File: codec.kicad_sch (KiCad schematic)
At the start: 23 parts, among them CN1 IN, CN2 OUT, U15 TAC5111IRGER, U17 LM321, U18 TPA6130A2RTJR

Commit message: wip 3.5mm audio jacks
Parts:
- added C50: 10nF, Capacitor_SMD:C_0402_1005Metric, symbol Device:C_Small
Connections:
- net GND: now also CN1.1
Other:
- moved on the sheet: CN1
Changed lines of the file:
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@@
 	(wire
 		(pts
+			(xy 38.1 162.56) (xy 40.64 162.56)
+		)
+		(stroke
+			(width 0)
+			(type default)
+		)
+	)
+	(wire
+		(pts
 			(xy 139.7 86.36) (xy 137.16 86.36)
 		)
@@
 	(symbol
 		(lib_id "custom:PJ-3537S")
-		(at 46.99 166.37 0)
+		(at 31.75 166.37 0)
 		(unit 1)
 		(body_style 1)
@@
 		(fields_autoplaced yes)
 		(property "Reference" "CN1"
-			(at 44.83 157.48 0)
+			(at 29.59 157.48 0)
 			(show_name no)
 			(do_not_autoplace no)
@@
 		)
 		(property "Value" "IN"
-			(at 44.83 160.02 0)
+			(at 29.59 160.02 0)
 			(show_name no)
 			(do_not_autoplace no)
@@
 		)
 		(property "Footprint" "custom:AUDIO-SMD_PJ-3537S"
-			(at 46.99 180.34 0)
+			(at 31.75 180.34 0)
 			(hide yes)
 			(show_name no)
@@
 		)
 		(property "Datasheet" "https://www.lcsc.com/datasheet/C2689709.pdf"
-			(at 46.99 182.88 0)
+			(at 31.75 182.88 0)
 			(hide yes)
 			(show_name no)
@@
 		)
 		(property "Description" ""
-			(at 46.99 166.37 0)
+			(at 31.75 166.37 0)
 			(hide yes)
 			(show_name no)
@@
 		)
 		(property "Manufacturer" "XKB Connection(中国星坤)"
-			(at 46.99 185.42 0)
+			(at 31.75 185.42 0)
 			(hide yes)
 			(show_name no)
@@
 		)
 		(property "MPN" "PJ-3537S-SMT"
-			(at 46.99 187.96 0)
+			(at 31.75 187.96 0)
 			(hide yes)
 			(show_name no)
@@
 		)
 		(property "LCSC Part" "C2689709"
-			(at 46.99 190.5 0)
+			(at 31.75 190.5 0)
 			(hide yes)
 			(show_name no)
@@
 		)
 		(property "LCSC" "C2689709"
-			(at 46.99 195.58 0)
+			(at 31.75 195.58 0)
 			(hide yes)
 			(show_name no)
@@
 	)
 	(symbol
+		(lib_id "Device:C_Small")
+		(at 66.04 185.42 90)
+		(unit 1)
+		(body_style 1)
+		(exclude_from_sim no)
+		(in_bom yes)
+		(on_board yes)
+		(in_pos_files yes)
+		(dnp no)
+		(property "Reference" "C50"
+			(at 66.0807 182.4637 90)
+			(show_name no)
+			(do_not_autoplace no)
+			(effects
+				(font
+					(size 1.27 1.27)
+				)
+			)
+		)
+		(property "Value" "10nF"
+			(at 66.0807 188.6269 90)
+			(show_name no)
+			(do_not_autoplace no)
+			(effects
+				(font
+					(size 1.27 1.27)
+				)
+			)
+		)
+		(property "Footprint" "Capacitor_SMD:C_0402_1005Metric"
+			(at 66.04 185.42 0)
+			(hide yes)
+			(show_name no)
+			(do_not_autoplace no)
+			(effects
+				(font
+					(size 1.27 1.27)
+				)
+			)
+		)
+		(property "Datasheet" ""
+			(at 66.04 185.42 0)
+			(hide yes)
+			(show_name no)
+			(do_not_autoplace no)
+			(effects
+				(font
+					(size 1.27 1.27)
+				)
+			)
+		)
+		(property "Description" "Unpolarized capacitor, small symbol"
+			(at 66.04 185.42 0)
+			(hide yes)
+			(show_name no)
+			(do_not_autoplace no)
+			(effects
+				(font
+					(size 1.27 1.27)
+				)
+			)
+		)
+		(property "LCSC" "C15195"
+			(at 66.04 185.42 0)
+			(hide yes)
+			(show_name no)
+			(do_not_autoplace no)
+			(effects
+				(font
+					(size 1.27 1.27)
+				)
+			)
+		)
+		(property "Voltage" "50V"
+			(at 66.04 185.42 90)
+			(hide yes)
+			(show_name no)
+			(do_not_autoplace no)
+			(effects
+				(font
+					(size 1.27 1.27)
+				)
+			)
+		)
+		(pin "1"
+		)
+		(pin "2"
+		)
+		(instances
+			(project "pedal"
+				(path "/e2443317-b83f-4e66-ac79-3186c6d613f3/a1bbde72-fd3e-4fef-8e82-ce5db1c82ed5"
+					(reference "C50")
+					(unit 1)
+				)
+			)
+		)
+	)
+	(symbol
 		(lib_id "power:GND")
 		(at 228.6 121.92 0)
@@
 	(symbol
 		(lib_id "power:GND")
-		(at 55.88 175.26 0)
-		(mirror y)
+		(at 40.64 162.56 90)
+		(mirror x)
 		(unit 1)
 		(body_style 1)
@@
 		(fields_autoplaced yes)
 		(property "Reference" "#PWR0135"
-			(at 55.88 181.61 0)
+			(at 46.99 162.56 0)
 			(hide yes)
 			(show_name no)
@@
 		)
 		(property "Value" "GND"
-			(at 55.88 180.34 0)
+			(at 44.45 162.5599 90)
 			(show_name no)
 			(do_not_autoplace no)
@@
 					(size 1.27 1.27)
 				)
+				(justify right)
 			)
 		)
 		(property "Footprint" ""
-			(at 55.88 175.26 0)
+			(at 40.64 162.56 0)
 			(hide yes)
 			(show_name no)
@@
 		)
 		(property "Datasheet" ""
-			(at 55.88 175.26 0)
+			(at 40.64 162.56 0)
 			(hide yes)
 			(show_name no)
@@
 		)
 		(property "Description" "Power symbol creates a global label with name \"GND\" , ground"
-			(at 55.88 175.26 0)
+			(at 40.64 162.56 0)
 			(hide yes)
 			(show_name no)

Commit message: FINALLY add 3.5mm audio jacks
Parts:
- removed CN1: IN, custom:AUDIO-SMD_PJ-3537S, symbol custom:PJ-3537S
- removed CN2: OUT, custom:AUDIO-SMD_PJ-3537S, symbol custom:PJ-3537S
- added C62, C63: 10nF, Capacitor_SMD:C_0402_1005Metric, symbol Device:C_Small
- added J10, J11, J9: PJ-327C-4A, custom:AUDIO-SMD_PJ-327C-4A, symbol custom:PJ-327C-4A
- added R28, R30, R31: 10k, Resistor_SMD:R_0402_1005Metric, symbol Device:R_Small
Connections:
- net GND: now also C50.2, C62.2, C63.2, J10.5 (S), J11.5 (S), J9.5 (S)
- net IN: now also J9.4 (T)
- net OUT_LEFT: now also J10.4 (T)
- net OUT_RIGHT: now also J11.4 (T)
- net at C50.1: now also J9.3 (DETECT), R28.1
- new net: C63.1, J11.3 (DETECT), R31.1
- new net: C62.1, J10.3 (DETECT), R30.1
- new net IN_DETECT: R28.2
- new net L_OUT_DETECT: R30.2
- new net R_OUT_DETECT: R31.2
- no-connect marks 5 -> 8

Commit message: OK ACTUALLY ADD JACKS
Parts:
- removed J10, J11, J9: PJ-327C-4A, custom:AUDIO-SMD_PJ-327C-4A, symbol custom:PJ-327C-4A
- added J7, J8, J9: PJ-342 141, custom:AUDIO-SMD_PJ-342-141, symbol custom:PJ-342141
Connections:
- net GND: now also J7.1 (GND), J8.1 (GND), J9.1 (GND)
- net at C63.1, R31.1: now also J9.2 (RING2)
- net at C62.1, R30.1: now also J8.2 (RING2)
- net at C50.1, R28.1: now also J7.2 (RING2)
- net IN: no longer names the net of C53.1
- net IN: now also J7.4 (TIP)
- net OUT_LEFT: no longer names the net of U18.14 (HPLEFT)
- net OUT_LEFT: now also J8.4 (TIP)
- net OUT_RIGHT: no longer names the net of U18.11 (HPRIGHT)
- net OUT_RIGHT: now also J9.4 (TIP)
- no-connect marks 8 -> 14
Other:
- note added: "Configure *_OUT_DETECT pins with internal pullups"
- moved on the sheet: C46, C47, C48, C49, C50, C51, C52, C53, C54, C55, C56, C58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

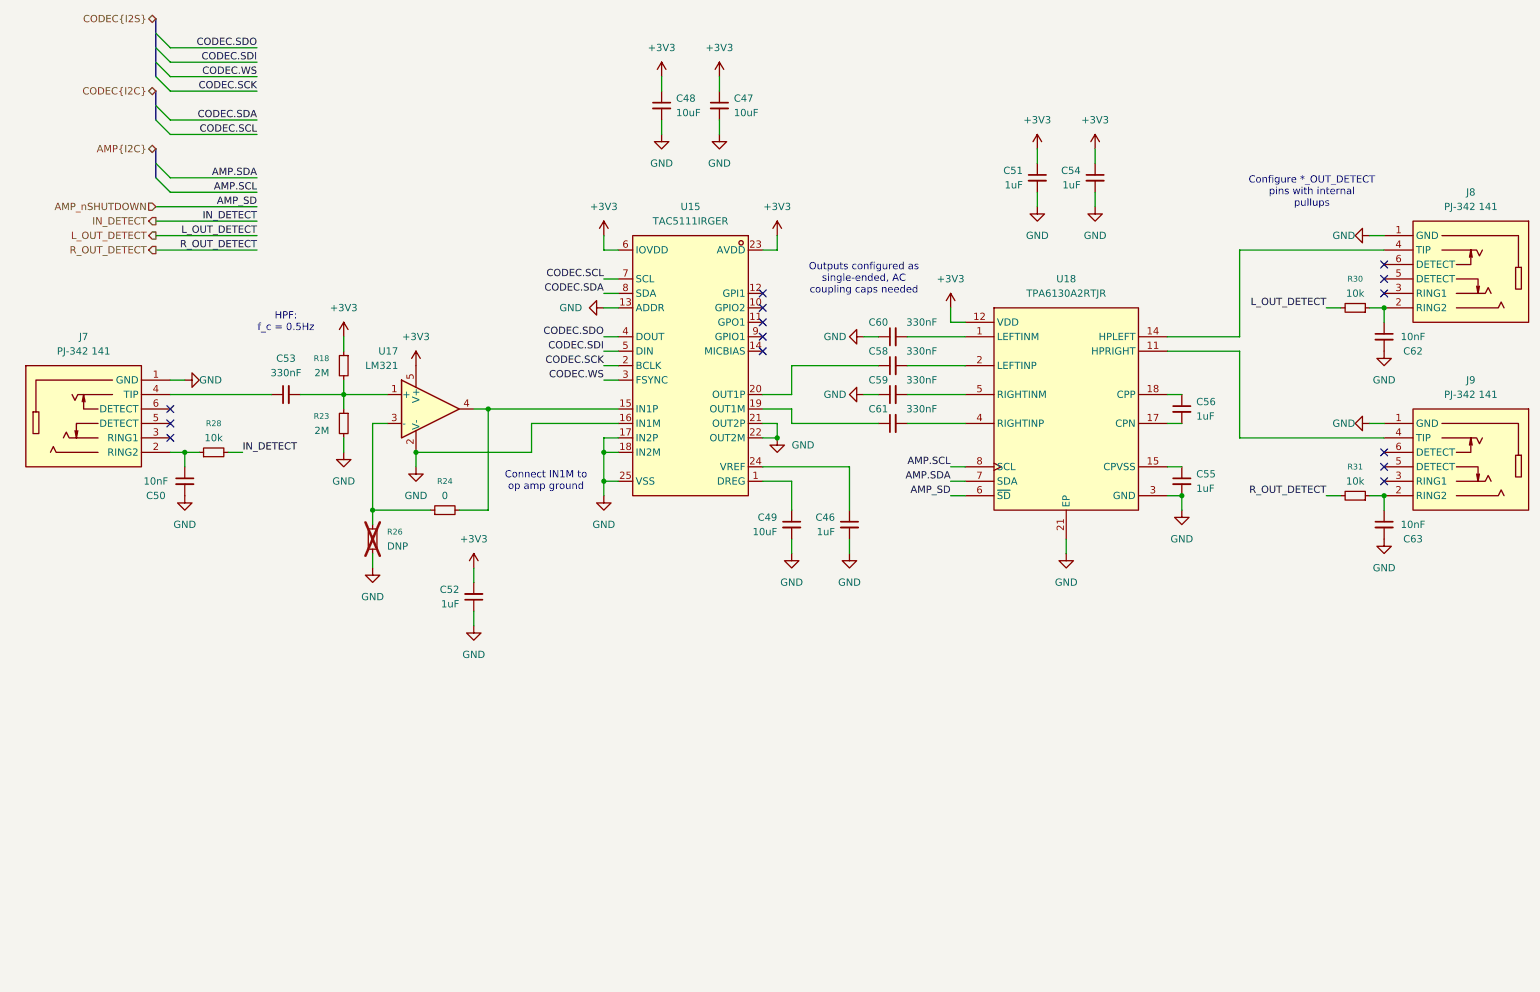
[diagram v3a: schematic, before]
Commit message: Input (#6)
* Add input subsheet
* Add debounce subsheet
* Add ultra thin buttons for ABXY
* Add start and select buttons
* Add L/R buttons
* Add joystick connector
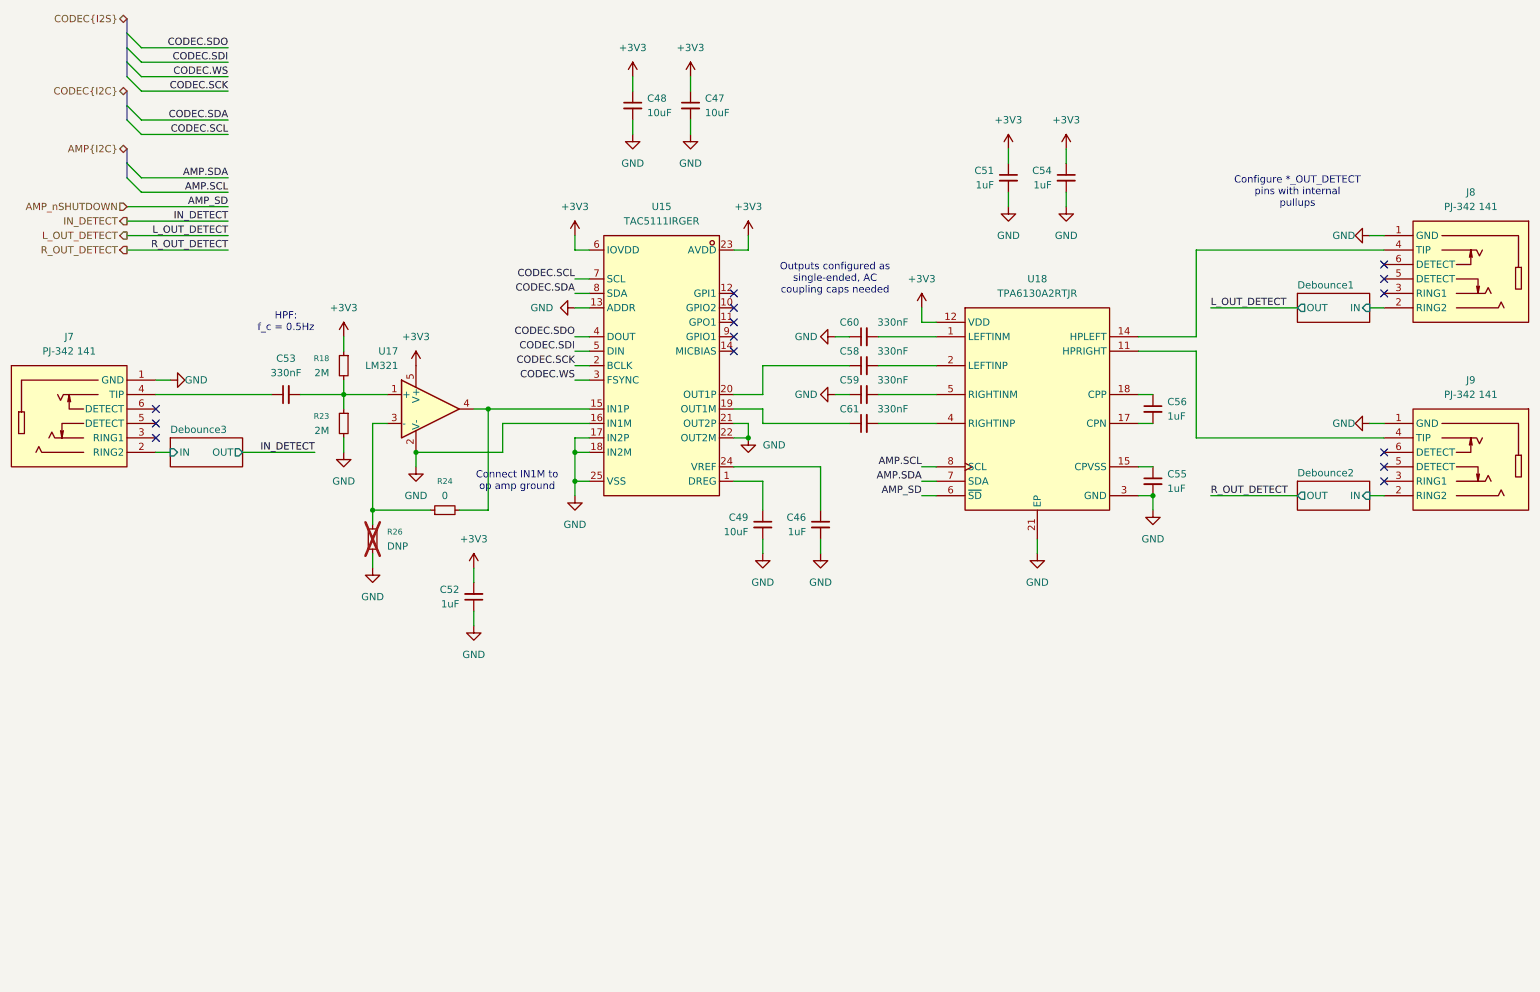
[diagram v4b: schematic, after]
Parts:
- removed C50, C62, C63: 10nF, Capacitor_SMD:C_0402_1005Metric, symbol Device:C_Small
- removed R28, R30, R31: 10k, Resistor_SMD:R_0402_1005Metric, symbol Device:R_Small
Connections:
- net Debounce2/IN: now reaches J9.2 (RING2)
- net Debounce1/IN: now reaches J8.2 (RING2)
- net Debounce3/IN: now reaches J7.2 (RING2)
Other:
- added sheet Debounce1 (debounce.kicad_sch)
- added sheet Debounce2 (debounce.kicad_sch)
- added sheet Debounce3 (debounce.kicad_sch)
- moved on the sheet: C46, C47, C48, C49, C51, C54, C55, C56, C58, C59, C60, C61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

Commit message: Move everything onto the board
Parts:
- J7: value PJ-342 141 -> IN
- J8: value PJ-342 141 -> L_OUT
- J9: value PJ-342 141 -> R_OUT
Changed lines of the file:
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@@
 		(in_pos_files yes)
 		(dnp no)
-		(fields_autoplaced yes)
 		(property "Reference" "J8"
-			(at 271.78 58.42 0)
-			(show_name no)
-			(do_not_autoplace no)
-			(effects
-				(font
-					(size 1.27 1.27)
-				)
-			)
-		)
-		(property "Value" "PJ-342 141"
-			(at 271.78 60.96 0)
-			(show_name no)
-			(do_not_autoplace no)
-			(effects
-				(font
-					(size 1.27 1.27)
-				)
+			(at 269.24 58.42 0)
+			(show_name no)
+			(do_not_autoplace no)
+			(effects
+				(font
+					(size 1.27 1.27)
+				)
+				(justify right)
+			)
+		)
+		(property "Value" "L_OUT"
+			(at 269.24 60.96 0)
+			(show_name no)
+			(do_not_autoplace no)
+			(effects
+				(font
+					(size 1.27 1.27)
+				)
+				(justify right)
 			)
 		)
@@
 			)
 		)
-		(property "Value" "PJ-342 141"
+		(property "Value" "IN"
 			(at 25.4 86.36 0)
 			(show_name no)
@@
 		(in_pos_files yes)
 		(dnp no)
-		(fields_autoplaced yes)
 		(property "Reference" "J9"
-			(at 271.78 91.44 0)
-			(show_name no)
-			(do_not_autoplace no)
-			(effects
-				(font
-					(size 1.27 1.27)
-				)
-			)
-		)
-		(property "Value" "PJ-342 141"
-			(at 271.78 93.98 0)
-			(show_name no)
-			(do_not_autoplace no)
-			(effects
-				(font
-					(size 1.27 1.27)
-				)
-			)
-		)
+			(at 269.24 91.44 0)
+			(show_name no)
+			(do_not_autoplace no)
+			(effects
+				(font
+					(size 1.27 1.27)
+				)
+				(justify right)
+			)
+		)
+		(property "Value" "R_OUT"
+			(at 269.24 93.98 0)
+			(show_name no)
+			(do_not_autoplace no)
+			(effects
+				(font
+					(size 1.27 1.27)
+				)
+				(justify right)
+			)
+		)
